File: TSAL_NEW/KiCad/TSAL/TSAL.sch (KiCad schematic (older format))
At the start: 20 parts, among them J1 HV INPUT, J2 HV GND, J3 Green_LED_Jp, J4 Conn_02x03_Counter_Clockwise, Q1 BSS84, Q2 FDD8447L, U1 LTV-817S, U2 LR8K4-G, U3 LM555, U4 LDB-350L

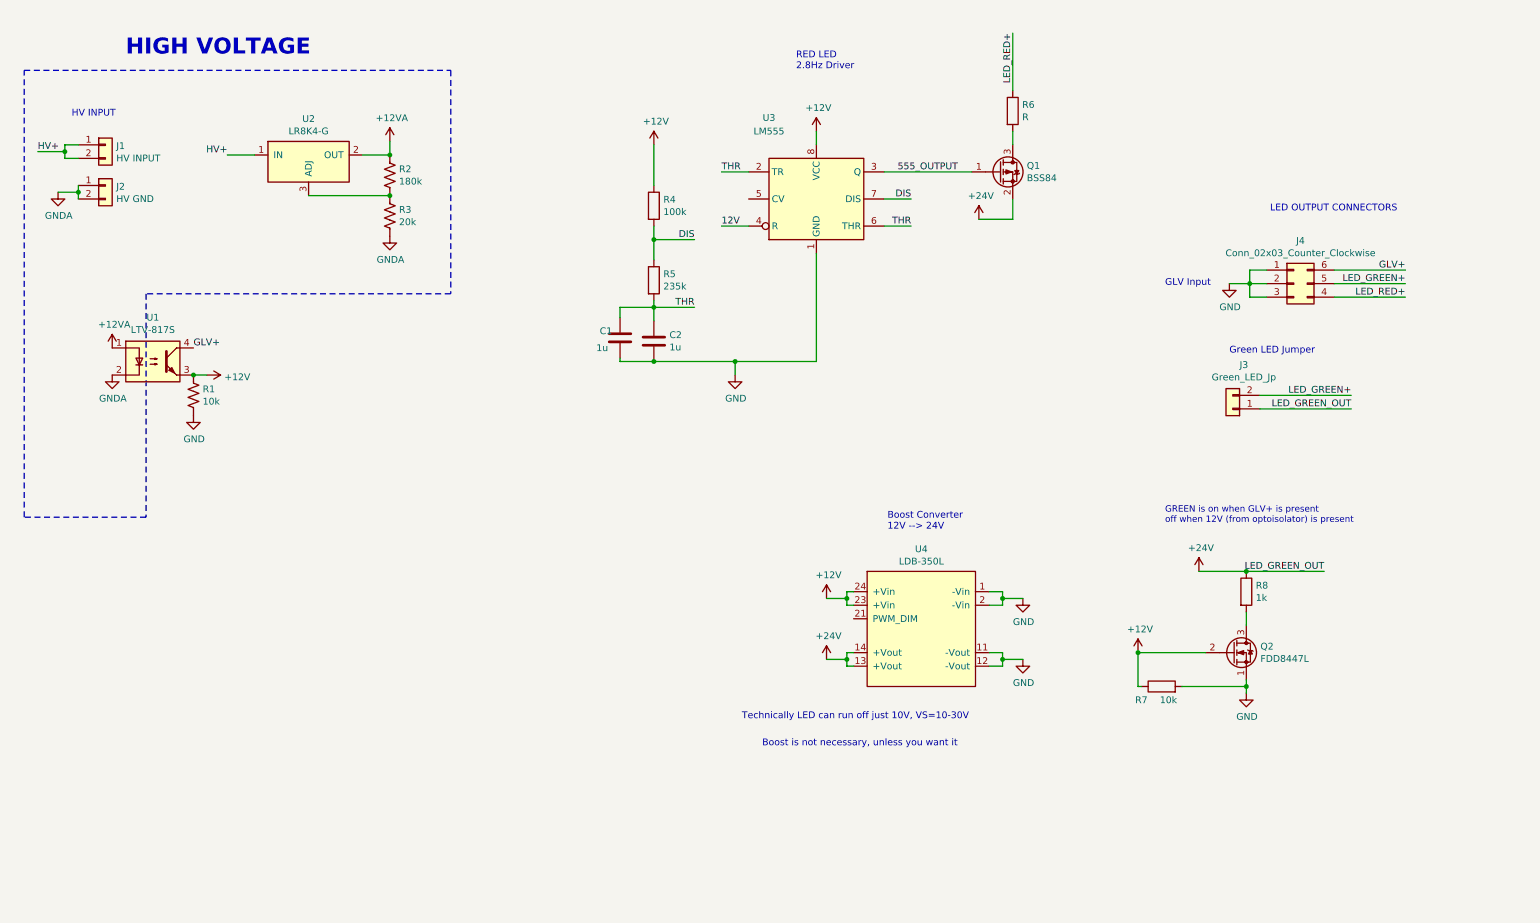
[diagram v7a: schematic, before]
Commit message: Suggested revisions of TSAL from review
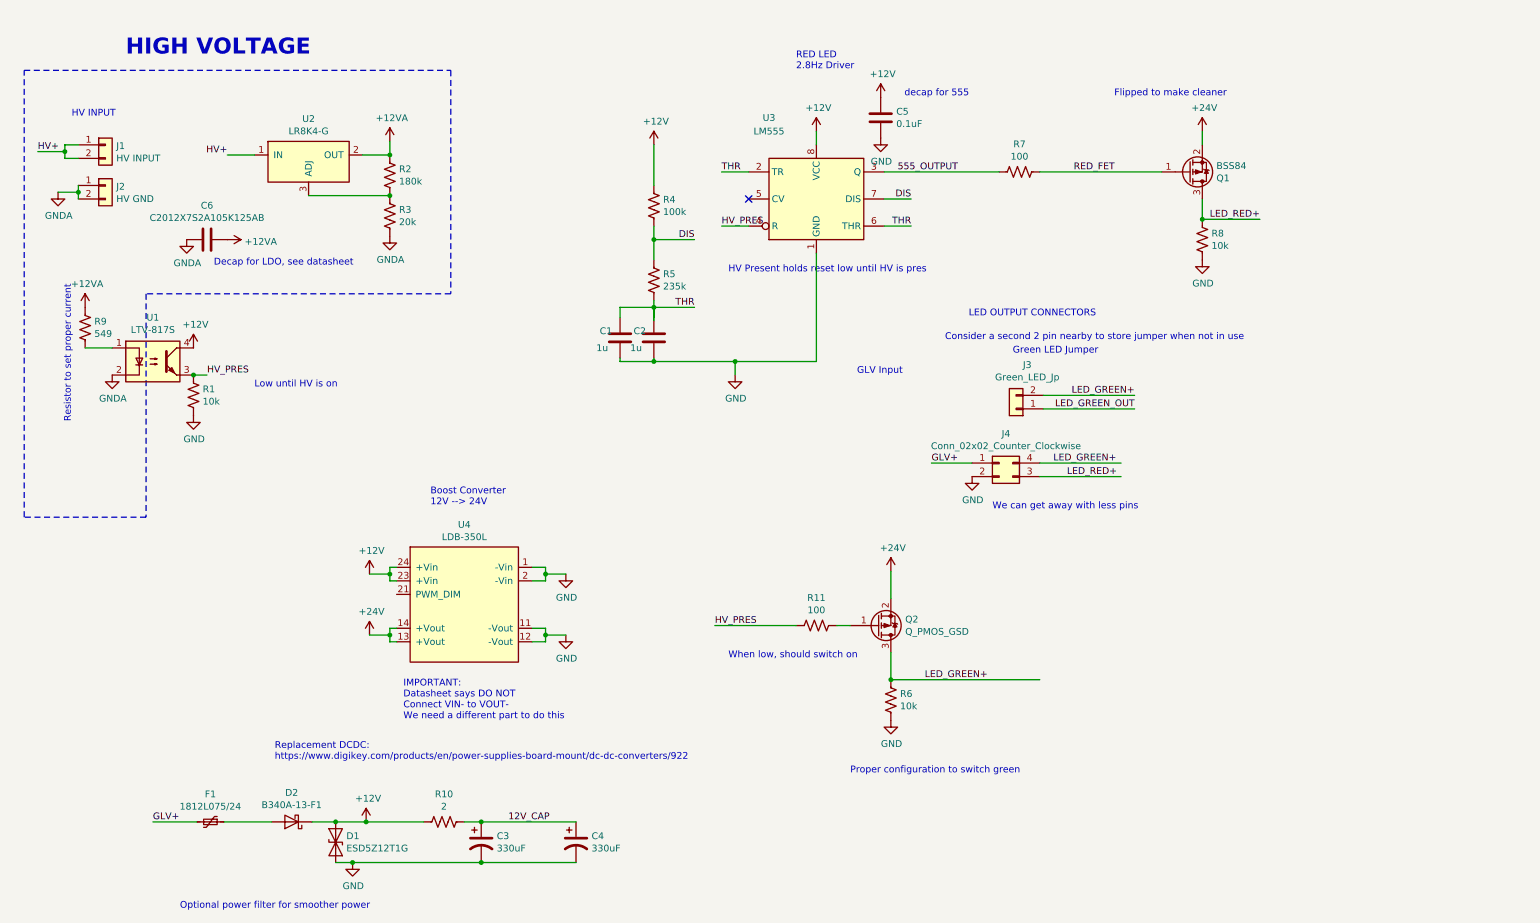
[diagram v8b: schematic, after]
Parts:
- removed J4: Conn_02x03_Counter_Clockwise, Connector_TE-Connectivity:TE_MATE-N-LOK_1-770875-x_2x03_P4.14mm_Vertical, symbol Connector_Generic:Conn_02x03_Counter_Clockwise
- removed Q2: FDD8447L, Package_TO_SOT_SMD:TO-252-2, symbol Transistor_FET:2N7000
- removed R4: 100k, Resistor_SMD:R_0603_1608Metric_Pad1.05x0.95mm_HandSolder, symbol Device:R
- removed R5: 235k, Resistor_SMD:R_0603_1608Metric_Pad1.05x0.95mm_HandSolder, symbol Device:R
- removed R6: R, Resistor_SMD:R_0603_1608Metric_Pad1.05x0.95mm_HandSolder, symbol Device:R
- removed R7: 10k, Resistor_SMD:R_0603_1608Metric_Pad1.05x0.95mm_HandSolder, symbol Device:R
- removed R8: 1k, Resistor_SMD:R_0603_1608Metric_Pad1.05x0.95mm_HandSolder, symbol Device:R
- added C3, C4: 330uF, Capacitor_SMD:CP_Elec_10x10, symbol Device:CP1
- added C5: 0.1uF, Capacitor_SMD:C_0603_1608Metric_Pad1.05x0.95mm_HandSolder, symbol Device:C
- added C6: C2012X7S2A105K125AB, Capacitor_SMD:C_0805_2012Metric, symbol Device:C
- added D1: ESD5Z12T1G, Diode_SMD:D_SMA_Handsoldering, symbol Device:D_TVS
- added D2: B340A-13-F1, Diode_SMD:D_SMA_Handsoldering, symbol Device:D_Schottky
- added F1: 1812L075/24, Fuse:Fuse_1812_4532Metric_Pad1.30x3.40mm_HandSolder, symbol Device:Polyfuse_Small
- added J4: Conn_02x02_Counter_Clockwise, Connector_TE-Connectivity:TE_MATE-N-LOK_1-770874-x_2x02_P4.14mm_Vertical, symbol Connector_Generic:Conn_02x02_Counter_Clockwise
- added Q2: Q_PMOS_GSD, symbol Device:Q_PMOS_GSD
- added R10: 2, Resistor_SMD:R_0603_1608Metric_Pad1.05x0.95mm_HandSolder, symbol Device:R_US
- added R11, R7: 100, Resistor_SMD:R_0603_1608Metric_Pad1.05x0.95mm_HandSolder, symbol Device:R_US
- added R4: 100k, Resistor_SMD:R_0603_1608Metric_Pad1.05x0.95mm_HandSolder, symbol Device:R_US
- added R5: 235k, Resistor_SMD:R_0603_1608Metric_Pad1.05x0.95mm_HandSolder, symbol Device:R_US
- added R6: 10k, symbol Device:R_US
- added R8: 10k, Resistor_SMD:R_0603_1608Metric_Pad1.05x0.95mm_HandSolder, symbol Device:R_US
- added R9: 549, Resistor_SMD:R_1210_3225Metric_Pad1.42x2.65mm_HandSolder, symbol Device:R_US
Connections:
- net labels added: 12V_CAP, HV_PRES, RED_FET
- net labels removed: 12V
- wire segments 78 -> 81
- no-connect marks 0 -> 1
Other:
- note added: "Consider a second 2 pin nearby to store jumper when not in use\n"
- note added: "Decap for LDO, see datasheet\n"
- note added: "Flipped to make cleaner\n"
- note added: "HV Present holds reset low until HV is pres\n"
- note added: "IMPORTANT:\nDatasheet says DO NOT\nConnect VIN- to VOUT-\nWe need a different part to do this"
- note added: "Low until HV is on\n"
- note added: "Optional power filter for smoother power\n"
- note added: "Proper configuration to switch green"
- note added: "Replacement DCDC:\nhttps://www.digikey.com/products/en/power-supplies-board-mount/dc-dc-converters/922"
- note added: "Resistor to set proper current\n"
- note added: "We can get away with less pins"
- note added: "When low, should switch on\n"
- note added: "decap for 555"
- note removed: "Boost is not necessary, unless you want it\n"
- note removed: "GREEN is on when GLV+ is present\noff when 12V (from optoisolator) is present"
- note removed: "Technically LED can run off just 10V, VS=10-30V"
- moved on the sheet: J3, Q1, U4
